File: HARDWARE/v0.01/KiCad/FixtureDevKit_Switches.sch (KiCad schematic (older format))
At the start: 58 parts, among them J10 LED_4, J11 SW_5, J12 LED_5, J13 SW_6, J14 LED_6, J15 SW_7, J2 LED_0, J3 SW_0, J4 SW_1, J5 LED_1, J6 SW_2, J7 LED_3, J8 SW_3, J9 SW_4, SW1 SW_Push_Dual, SW2 SW_Push_Dual, SW3 SW_Push_Dual, SW4 SW_Push_Dual, SW5 SW_Push_Dual, SW6 SW_Push_Dual, SW7 SW_Push_Dual, SW8 SW_Push_Dual

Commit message: adding datasheets
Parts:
- D1, D11, D3, D5, D7: value LED -> Purple
- D12, D2, D4, D6, D8: value LED -> Green
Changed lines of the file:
@@
 P 2150 2650
 F 0 "D2" H 2150 2750 50  0000 C CNN
-F 1 "LED" H 2150 2550 50  0000 C CNN
+F 1 "Green" H 2150 2550 50  0000 C CNN
 F 2 "LEDs:LED_0805_HandSoldering" H 2150 2650 50  0001 C CNN
 F 3 "" H 2150 2650 50  0001 C CNN
@@
 P 2150 2350
 F 0 "D1" H 2150 2450 50  0000 C CNN
-F 1 "LED" H 2150 2250 50  0000 C CNN
+F 1 "Purple" H 2150 2250 50  0000 C CNN
 F 2 "LEDs:LED_0805_HandSoldering" H 2150 2350 50  0001 C CNN
 F 3 "" H 2150 2350 50  0001 C CNN
@@
 P 3600 2650
 F 0 "D4" H 3600 2750 50  0000 C CNN
-F 1 "LED" H 3600 2550 50  0000 C CNN
+F 1 "Green" H 3600 2550 50  0000 C CNN
 F 2 "LEDs:LED_0805_HandSoldering" H 3600 2650 50  0001 C CNN
 F 3 "" H 3600 2650 50  0001 C CNN
@@
 P 3600 2350
 F 0 "D3" H 3600 2450 50  0000 C CNN
-F 1 "LED" H 3600 2250 50  0000 C CNN
+F 1 "Purple" H 3600 2250 50  0000 C CNN
 F 2 "LEDs:LED_0805_HandSoldering" H 3600 2350 50  0001 C CNN
 F 3 "" H 3600 2350 50  0001 C CNN
@@
 P 5000 2650
 F 0 "D6" H 5000 2750 50  0000 C CNN
-F 1 "LED" H 5000 2550 50  0000 C CNN
+F 1 "Green" H 5000 2550 50  0000 C CNN
 F 2 "LEDs:LED_0805_HandSoldering" H 5000 2650 50  0001 C CNN
 F 3 "" H 5000 2650 50  0001 C CNN
@@
 P 5000 2350
 F 0 "D5" H 5000 2450 50  0000 C CNN
-F 1 "LED" H 5000 2250 50  0000 C CNN
+F 1 "Purple" H 5000 2250 50  0000 C CNN
 F 2 "LEDs:LED_0805_HandSoldering" H 5000 2350 50  0001 C CNN
 F 3 "" H 5000 2350 50  0001 C CNN
@@
 P 6450 2650
 F 0 "D8" H 6450 2750 50  0000 C CNN
-F 1 "LED" H 6450 2550 50  0000 C CNN
+F 1 "Green" H 6450 2550 50  0000 C CNN
 F 2 "LEDs:LED_0805_HandSoldering" H 6450 2650 50  0001 C CNN
 F 3 "" H 6450 2650 50  0001 C CNN
@@
 P 6450 2350
 F 0 "D7" H 6450 2450 50  0000 C CNN
-F 1 "LED" H 6450 2250 50  0000 C CNN
+F 1 "Purple" H 6450 2250 50  0000 C CNN
 F 2 "LEDs:LED_0805_HandSoldering" H 6450 2350 50  0001 C CNN
 F 3 "" H 6450 2350 50  0001 C CNN
@@
 P 9300 2650
 F 0 "D12" H 9300 2750 50  0000 C CNN
-F 1 "LED" H 9300 2550 50  0000 C CNN
+F 1 "Green" H 9300 2550 50  0000 C CNN
 F 2 "LEDs:LED_0805_HandSoldering" H 9300 2650 50  0001 C CNN
 F 3 "" H 9300 2650 50  0001 C CNN
@@
 P 9300 2350
 F 0 "D11" H 9300 2450 50  0000 C CNN
-F 1 "LED" H 9300 2250 50  0000 C CNN
+F 1 "Purple" H 9300 2250 50  0000 C CNN
 F 2 "LEDs:LED_0805_HandSoldering" H 9300 2350 50  0001 C CNN
 F 3 "" H 9300 2350 50  0001 C CNN

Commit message: beginning pcb layout
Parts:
- removed TP1, TP11, TP9: VS, TestPoint:TestPoint, symbol TEST
- removed TP10, TP12: SIG, TestPoint:TestPoint, symbol TEST
- added D15, D17: Purple, LEDs:LED_0805_HandSoldering, symbol LED
- added D16, D18: Green, LEDs:LED_0805_HandSoldering, symbol LED
- added J106: LED_6, Pin_Headers:Pin_Header_Straight_1x03_Pitch2.54mm, symbol Conn_01x03
- added J107: LED_7, Pin_Headers:Pin_Header_Straight_1x03_Pitch2.54mm, symbol Conn_01x03
- added R96, R97, R98, R99: 1K, Resistors_SMD:R_0805_HandSoldering, symbol R
- added TP2: SIG, TestPoint:TestPoint, symbol TEST
- D10: value LED -> Green
- D9: value LED -> Purple
- J10: value LED_4 -> LED_3
- J12: value LED_5 -> LED_4
- J14: value LED_6 -> LED_5
- J7: value LED_3 -> LED_2
- TP3, TP5, TP7: value VS -> SIG
- renumbered TP2 to TP1
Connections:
- net GND: now also J106.3 (Pin_3), J107.3 (Pin_3), R97.1, R99.1
- net at D2.1 (K), R2.2: no longer D1.2 (A), R1.1
- net at D3.1 (K), D4.2 (A), J5.2 (Pin_2): now also TP2.1; no longer TP4.1
- net at D5.1 (K), D6.2 (A), J7.2 (Pin_2): now also TP3.1; no longer TP6.1
- net at D7.1 (K), D8.2 (A), J10.2 (Pin_2): now also TP4.1; no longer TP8.1
- net at D10.2 (A), D9.1 (K), J12.2 (Pin_2): now also TP5.1
- net at D10.1 (K), R10.2: no longer D9.2 (A), R9.1
- net at D11.1 (K), D12.2 (A), J14.2 (Pin_2): now also TP6.1
- net at D12.1 (K), R12.2: no longer D11.2 (A), R11.1
- new net: D1.2 (A), R1.1
- new net: D4.1 (K), R4.2
- new net: D3.2 (A), R3.1
- new net: D6.1 (K), R6.2
- new net: D5.2 (A), R5.1
- new net: D8.1 (K), R8.2
- new net: D7.2 (A), R7.1
- new net: D9.2 (A), R9.1
- new net: D11.2 (A), R11.1
- new net: J106.1 (Pin_1), R96.2
- new net: D15.1 (K), D16.2 (A), J106.2 (Pin_2), TP7.1
- new net: D16.1 (K), R97.2
- new net: D15.2 (A), R96.1
- new net: J107.1 (Pin_1), R98.2
- new net: D17.1 (K), D18.2 (A), J107.2 (Pin_2), TP8.1
- new net: D18.1 (K), R99.2
- new net: D17.2 (A), R98.1
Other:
- moved on the sheet: D1, D2, J2, R1, R2, TP1

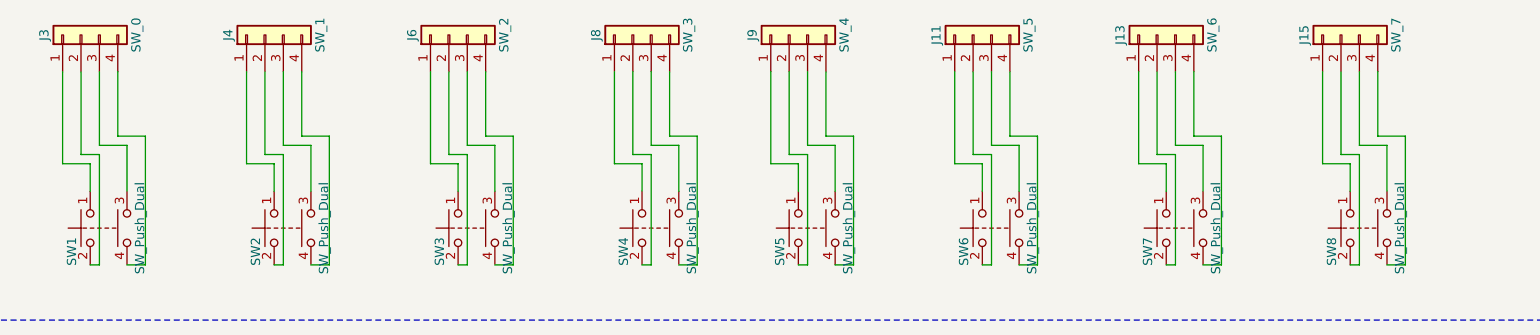
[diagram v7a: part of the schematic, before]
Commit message: adding datasheets and laying out PCB
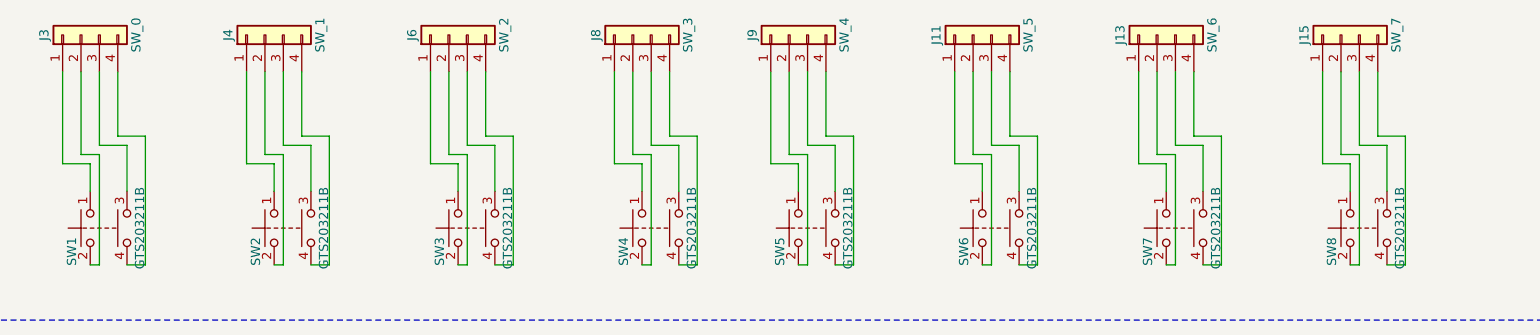
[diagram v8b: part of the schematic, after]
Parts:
- SW1, SW2, SW3, SW4, SW5, SW6, SW7, SW8: value SW_Push_Dual -> GTS203211B
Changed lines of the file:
@@
 LIBS:valves
 LIBS:TCA6424ARGJR
+LIBS:USB-A1HSW6
 LIBS:Fixture-Dev-Kit-cache
 EELAYER 25 0
@@
 P 2300 5750
 F 0 "SW1" H 2350 5850 50  0000 L CNN
-F 1 "SW_Push_Dual" H 2300 5480 50  0000 C CNN
+F 1 "GTS203211B" H 2300 5480 50  0000 C CNN
 F 2 "" H 2300 5950 50  0001 C CNN
 F 3 "" H 2300 5950 50  0001 C CNN
@@
 P 3300 5750
 F 0 "SW2" H 3350 5850 50  0000 L CNN
-F 1 "SW_Push_Dual" H 3300 5480 50  0000 C CNN
+F 1 "GTS203211B" H 3300 5480 50  0000 C CNN
 F 2 "" H 3300 5950 50  0001 C CNN
 F 3 "" H 3300 5950 50  0001 C CNN
@@
 P 4300 5750
 F 0 "SW3" H 4350 5850 50  0000 L CNN
-F 1 "SW_Push_Dual" H 4300 5480 50  0000 C CNN
+F 1 "GTS203211B" H 4300 5480 50  0000 C CNN
 F 2 "" H 4300 5950 50  0001 C CNN
 F 3 "" H 4300 5950 50  0001 C CNN
@@
 P 5300 5750
 F 0 "SW4" H 5350 5850 50  0000 L CNN
-F 1 "SW_Push_Dual" H 5300 5480 50  0000 C CNN
+F 1 "GTS203211B" H 5300 5480 50  0000 C CNN
 F 2 "" H 5300 5950 50  0001 C CNN
 F 3 "" H 5300 5950 50  0001 C CNN
@@
 P 6150 5750
 F 0 "SW5" H 6200 5850 50  0000 L CNN
-F 1 "SW_Push_Dual" H 6150 5480 50  0000 C CNN
+F 1 "GTS203211B" H 6150 5480 50  0000 C CNN
 F 2 "" H 6150 5950 50  0001 C CNN
 F 3 "" H 6150 5950 50  0001 C CNN
@@
 P 7150 5750
 F 0 "SW6" H 7200 5850 50  0000 L CNN
-F 1 "SW_Push_Dual" H 7150 5480 50  0000 C CNN
+F 1 "GTS203211B" H 7150 5480 50  0000 C CNN
 F 2 "" H 7150 5950 50  0001 C CNN
 F 3 "" H 7150 5950 50  0001 C CNN
@@
 P 8150 5750
 F 0 "SW7" H 8200 5850 50  0000 L CNN
-F 1 "SW_Push_Dual" H 8150 5480 50  0000 C CNN
+F 1 "GTS203211B" H 8150 5480 50  0000 C CNN
 F 2 "" H 8150 5950 50  0001 C CNN
 F 3 "" H 8150 5950 50  0001 C CNN
@@
 P 9150 5750
 F 0 "SW8" H 9200 5850 50  0000 L CNN
-F 1 "SW_Push_Dual" H 9150 5480 50  0000 C CNN
+F 1 "GTS203211B" H 9150 5480 50  0000 C CNN
 F 2 "" H 9150 5950 50  0001 C CNN
 F 3 "" H 9150 5950 50  0001 C CNN
